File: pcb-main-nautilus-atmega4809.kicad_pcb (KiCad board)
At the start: 4 copper layers, 68.6 x 53.3 mm, 110 parts, among them J1 694106301002, J2 105017-0001, J3 FTSH-105-01-L-DV-007-K, J4 75844-101-06LF, J5 66951-006LF, J6 66951-010LF, J7 66951-008LF, J8 66951-008LF, Q1 BSS138PW, Q2 BSS138PW, Q3 BSS138PW, SW1 PTS645SH43SMTR92 LFS, U1 NCP1117-5.0_TO252, U2 AP2112K-3.3, U3 ATSAMD11D14A-SS, U4 ATmega4809-A

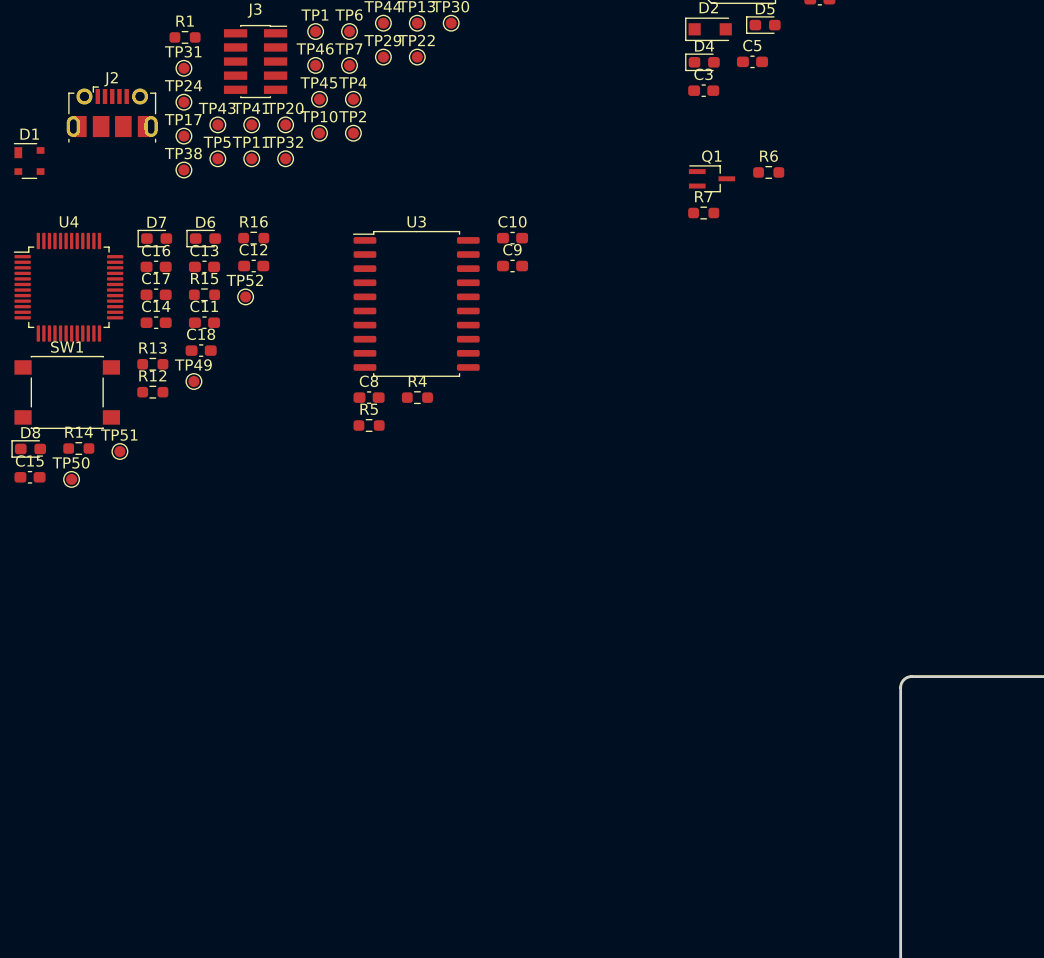
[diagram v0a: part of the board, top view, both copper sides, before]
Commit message: Place USB connector
Supports #4.
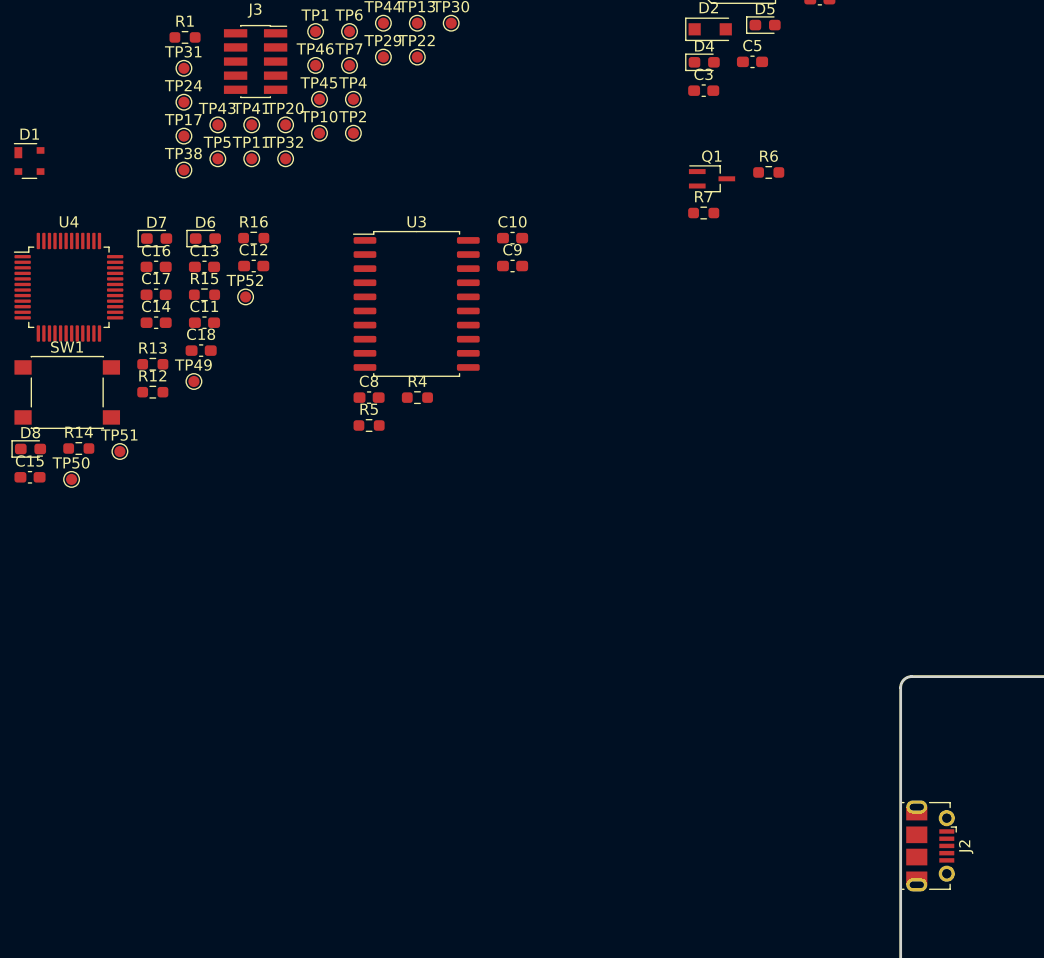
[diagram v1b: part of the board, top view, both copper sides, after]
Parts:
- moved J2 98.9 mm to (102.7, 111.9), turned to -90 degrees
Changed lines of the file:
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@@
     )
   )
-  (footprint "Connector_USB:USB_Micro-B_Molex-105017-0001" (layer "F.Cu")
-    (at 29.06 45.93)
+  (footprint "Connector_USB:USB_Micro-B_Molex-105017-0001" locked (layer "F.Cu")
+    (at 102.689204 111.9 -90)
     (descr "http://www.molex.com/pdm_docs/sd/1050170001_sd.pdf")
     (tags "Micro-USB SMD Typ-B")
@@
     (property "Sheetname" "")
     (attr smd)
-    (fp_text reference "J2" (at 0 -3.1125) (layer "F.SilkS")
+    (fp_text reference "J2" (at 0 -3.1125 90) (layer "F.SilkS")
       (effects (font (size 1 1) (thickness 0.15)))
     )
-    (fp_text value "105017-0001" (at 0.3 4.3375) (layer "F.Fab")
+    (fp_text value "105017-0001" (at 0.3 4.3375 90) (layer "F.Fab")
       (effects (font (size 1 1) (thickness 0.15)))
     )
-    (fp_text user "PCB Edge" (at 0 2.6875) (layer "Dwgs.User")
+    (fp_text user "PCB Edge" (at 0 2.6875 90) (layer "Dwgs.User")
       (effects (font (size 0.5 0.5) (thickness 0.08)))
     )
-    (fp_text user "${REFERENCE}" (at 0 0.8875) (layer "F.Fab")
+    (fp_text user "${REFERENCE}" (at 0 0.8875 90) (layer "F.Fab")
       (effects (font (size 1 1) (thickness 0.15)))
     )
@@
     (fp_line (start -1.1 -2.1225) (end -1.1 -1.9125) (layer "F.Fab") (width 0.1))
     (fp_line (start -3.75 -1.6125) (end 3.75 -1.6125) (layer "F.Fab") (width 0.1))
-    (pad "1" smd rect (at -1.3 -1.4625) (size 0.4 1.35) (layers "F.Cu" "F.Paste" "F.Mask")
+    (pad "1" smd rect locked (at -1.3 -1.4625 270) (size 0.4 1.35) (layers "F.Cu" "F.Paste" "F.Mask")
       (net 11 "/POWER/USB_VBUS") (pinfunction "VBUS") (pintype "power_out"))
-    (pad "2" smd rect (at -0.65 -1.4625) (size 0.4 1.35) (layers "F.Cu" "F.Paste" "F.Mask")
+    (pad "2" smd rect locked (at -0.65 -1.4625 270) (size 0.4 1.35) (layers "F.Cu" "F.Paste" "F.Mask")
       (net 9 "/UPDI PROGRAMMER AND USB-SERIAL BRIDGE/USB_D-") (pinfunction "D-") (pintype "bidirectional"))
-    (pad "3" smd rect (at 0 -1.4625) (size 0.4 1.35) (layers "F.Cu" "F.Paste" "F.Mask")
+    (pad "3" smd rect locked (at 0 -1.4625 270) (size 0.4 1.35) (layers "F.Cu" "F.Paste" "F.Mask")
       (net 10 "/UPDI PROGRAMMER AND USB-SERIAL BRIDGE/USB_D+") (pinfunction "D+") (pintype "bidirectional"))
-    (pad "4" smd rect (at 0.65 -1.4625) (size 0.4 1.35) (layers "F.Cu" "F.Paste" "F.Mask")
+    (pad "4" smd rect locked (at 0.65 -1.4625 270) (size 0.4 1.35) (layers "F.Cu" "F.Paste" "F.Mask")
       (net 19 "unconnected-(J2-Pad4)") (pinfunction "ID") (pintype "passive+no_connect"))
-    (pad "5" smd rect (at 1.3 -1.4625) (size 0.4 1.35) (layers "F.Cu" "F.Paste" "F.Mask")
+    (pad "5" smd rect locked (at 1.3 -1.4625 270) (size 0.4 1.35) (layers "F.Cu" "F.Paste" "F.Mask")
       (net 2 "/GND") (pinfunction "GND") (pintype "power_out"))
-    (pad "6" smd rect (at -1 1.2375) (size 1.5 1.9) (layers "F.Cu" "F.Paste" "F.Mask")
+    (pad "6" smd rect locked (at -1 1.2375 270) (size 1.5 1.9) (layers "F.Cu" "F.Paste" "F.Mask")
       (net 1 "Net-(C1-Pad1)") (pinfunction "Shield") (pintype "passive"))
-    (pad "6" smd rect (at 2.9 1.2375) (size 1.2 1.9) (layers "F.Cu" "F.Mask")
+    (pad "6" smd rect locked (at 2.9 1.2375 270) (size 1.2 1.9) (layers "F.Cu" "F.Mask")
       (net 1 "Net-(C1-Pad1)") (pinfunction "Shield") (pintype "passive"))
-    (pad "6" thru_hole oval (at 3.5 1.2375) (size 1.2 1.9) (drill oval 0.6 1.3) (layers *.Cu *.Mask)
+    (pad "6" thru_hole oval locked (at 3.5 1.2375 270) (size 1.2 1.9) (drill oval 0.6 1.3) (layers *.Cu *.Mask)
       (net 1 "Net-(C1-Pad1)") (pinfunction "Shield") (pintype "passive"))
-    (pad "6" smd rect (at 1 1.2375) (size 1.5 1.9) (layers "F.Cu" "F.Paste" "F.Mask")
+    (pad "6" smd rect locked (at 1 1.2375 270) (size 1.5 1.9) (layers "F.Cu" "F.Paste" "F.Mask")
       (net 1 "Net-(C1-Pad1)") (pinfunction "Shield") (pintype "passive"))
-    (pad "6" thru_hole circle (at 2.5 -1.4625) (size 1.45 1.45) (drill 0.85) (layers *.Cu *.Mask)
+    (pad "6" thru_hole circle locked (at 2.5 -1.4625 270) (size 1.45 1.45) (drill 0.85) (layers *.Cu *.Mask)
       (net 1 "Net-(C1-Pad1)") (pinfunction "Shield") (pintype "passive"))
-    (pad "6" thru_hole circle (at -2.5 -1.4625) (size 1.45 1.45) (drill 0.85) (layers *.Cu *.Mask)
+    (pad "6" thru_hole circle locked (at -2.5 -1.4625 270) (size 1.45 1.45) (drill 0.85) (layers *.Cu *.Mask)
       (net 1 "Net-(C1-Pad1)") (pinfunction "Shield") (pintype "passive"))
-    (pad "6" thru_hole oval (at -3.5 1.2375 180) (size 1.2 1.9) (drill oval 0.6 1.3) (layers *.Cu *.Mask)
+    (pad "6" thru_hole oval locked (at -3.5 1.2375 90) (size 1.2 1.9) (drill oval 0.6 1.3) (layers *.Cu *.Mask)
       (net 1 "Net-(C1-Pad1)") (pinfunction "Shield") (pintype "passive"))
-    (pad "6" smd rect (at -2.9 1.2375) (size 1.2 1.9) (layers "F.Cu" "F.Mask")
+    (pad "6" smd rect locked (at -2.9 1.2375 270) (size 1.2 1.9) (layers "F.Cu" "F.Mask")
       (net 1 "Net-(C1-Pad1)") (pinfunction "Shield") (pintype "passive"))
     (model "${KICAD6_3DMODEL_DIR}/Connector_USB.3dshapes/USB_Micro-B_Molex-105017-0001.wrl"

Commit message: Group components
Supports #4.
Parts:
- moved D8 239.4 mm to (260.4, 95.2)
- moved TP52 224.0 mm to (260.4, 108.0)
- moved R16 223.0 mm to (260.4, 101.6)
- moved TP51 220.2 mm to (247.7, 108.0)
- moved D7 218.8 mm to (248.5, 95.2)
- moved TP24 215.1 mm to (228.6, 139.7)
- moved R15 213.9 mm to (247.7, 101.6)
- moved TP50 211.6 mm to (234.9, 108.0)
- moved R14 211.4 mm to (235.9, 101.6)
- moved TP21 203.2 mm to (196.8, 171.4)
- moved D6 202.0 mm to (235.8, 95.2)
- moved TP23 199.7 mm to (228.6, 133.3)
- moved TP20 192.6 mm to (196.8, 165.1)
- moved SW1 192.4 mm to (215.9, 95.2)
- moved R13 188.8 mm to (215.9, 114.3)
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
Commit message: Add missing test points
Supports #4.
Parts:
- added TP49: TestPoint, TestPoint:TestPoint_Pad_D1.0mm, F.Cu at (171.4, 76.2)
- added TP50: TestPoint, TestPoint:TestPoint_Pad_D1.0mm, F.Cu at (171.4, 82.5)
- added TP51: TestPoint, TestPoint:TestPoint_Pad_D1.0mm, F.Cu at (171.4, 88.9)
- renumbered TP49 to TP52, TP50 to TP53, TP51 to TP54, TP52 to TP55
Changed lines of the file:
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@@
     (property "Sheetname" "MCU")
     (attr exclude_from_pos_files)
-    (fp_text reference "TP52" (at 0 -1.448) (layer "F.SilkS")
+    (fp_text reference "TP55" (at 0 -1.448) (layer "F.SilkS")
       (effects (font (size 1 1) (thickness 0.15)))
     )
@@
     (pad "1" smd circle (at 0 0) (size 1 1) (layers "F.Cu" "F.Mask")
       (net 41 "/MCU/D7") (pinfunction "1") (pintype "passive"))
+  )
+  (footprint "TestPoint:TestPoint_Pad_D1.0mm" (layer "F.Cu")
+    (at 171.45 82.55)
+    (descr "SMD pad as test Point, diameter 1.0mm")
+    (tags "test point SMD pad")
+    (property "Sheetfile" "pcb-main-nautilus-atmega4809-sheet-updi_programmer_and_usb_serial_bridge.kicad_sch")
+    (property "Sheetname" "UPDI PROGRAMMER AND USB-SERIAL BRIDGE")
+    (attr exclude_from_pos_files)
+    (fp_text reference "TP50" (at 0 -1.448) (layer "F.SilkS")
+      (effects (font (size 1 1) (thickness 0.15)))
+    )
+    (fp_text value "TestPoint" (at 0 1.55) (layer "F.Fab")
+      (effects (font (size 1 1) (thickness 0.15)))
+    )
+    (fp_text user "${REFERENCE}" (at 0 -1.45) (layer "F.Fab")
+      (effects (font (size 1 1) (thickness 0.15)))
+    )
+    (fp_circle (center 0 0) (end 0 0.7) (layer "F.SilkS") (width 0.12) (fill none))
+    (fp_circle (center 0 0) (end 1 0) (layer "F.CrtYd") (width 0.05) (fill none))
+    (pad "1" smd circle (at 0 0) (size 1 1) (layers "F.Cu" "F.Mask")
+      (net 51 "/UPDI PROGRAMMER AND USB-SERIAL BRIDGE/BI-DIRECTIONAL LEVEL SHIFTER: TX/SIGNAL_3.3V") (pinfunction "1") (pintype "passive"))
   )
   (footprint "Package_TO_SOT_SMD:SOT-23-5" (layer "F.Cu")
@@
     (property "Sheetname" "MCU")
     (attr exclude_from_pos_files)
-    (fp_text reference "TP51" (at 0 -1.448) (layer "F.SilkS")
+    (fp_text reference "TP54" (at 0 -1.448) (layer "F.SilkS")
       (effects (font (size 1 1) (thickness 0.15)))
     )
@@
   )
   (footprint "TestPoint:TestPoint_Pad_D1.0mm" (layer "F.Cu")
+    (at 171.45 88.9)
+    (descr "SMD pad as test Point, diameter 1.0mm")
+    (tags "test point SMD pad")
+    (property "Sheetfile" "pcb-main-nautilus-atmega4809-sheet-updi_programmer_and_usb_serial_bridge.kicad_sch")
+    (property "Sheetname" "UPDI PROGRAMMER AND USB-SERIAL BRIDGE")
+    (attr exclude_from_pos_files)
+    (fp_text reference "TP51" (at 0 -1.448) (layer "F.SilkS")
+      (effects (font (size 1 1) (thickness 0.15)))
+    )
+    (fp_text value "TestPoint" (at 0 1.55) (layer "F.Fab")
+      (effects (font (size 1 1) (thickness 0.15)))
+    )
+    (fp_text user "${REFERENCE}" (at 0 -1.45) (layer "F.Fab")
+      (effects (font (size 1 1) (thickness 0.15)))
+    )
+    (fp_circle (center 0 0) (end 0 0.7) (layer "F.SilkS") (width 0.12) (fill none))
+    (fp_circle (center 0 0) (end 1 0) (layer "F.CrtYd") (width 0.05) (fill none))
+    (pad "1" smd circle (at 0 0) (size 1 1) (layers "F.Cu" "F.Mask")
+      (net 50 "/UPDI PROGRAMMER AND USB-SERIAL BRIDGE/BI-DIRECTIONAL LEVEL SHIFTER: UPDI/SIGNAL_3.3V") (pinfunction "1") (pintype "passive"))
+  )
+  (footprint "TestPoint:TestPoint_Pad_D1.0mm" (layer "F.Cu")
     (at 19.05 82.55)
     (descr "SMD pad as test Point, diameter 1.0mm")
@@
   )
   (footprint "TestPoint:TestPoint_Pad_D1.0mm" (layer "F.Cu")
+    (at 171.45 76.2)
+    (descr "SMD pad as test Point, diameter 1.0mm")
+    (tags "test point SMD pad")
+    (property "Sheetfile" "pcb-main-nautilus-atmega4809-sheet-updi_programmer_and_usb_serial_bridge.kicad_sch")
+    (property "Sheetname" "UPDI PROGRAMMER AND USB-SERIAL BRIDGE")
+    (attr exclude_from_pos_files)
+    (fp_text reference "TP49" (at 0 -1.448) (layer "F.SilkS")
+      (effects (font (size 1 1) (thickness 0.15)))
+    )
+    (fp_text value "TestPoint" (at 0 1.55) (layer "F.Fab")
+      (effects (font (size 1 1) (thickness 0.15)))
+    )
+    (fp_text user "${REFERENCE}" (at 0 -1.45) (layer "F.Fab")
+      (effects (font (size 1 1) (thickness 0.15)))
+    )
+    (fp_circle (center 0 0) (end 0 0.7) (layer "F.SilkS") (width 0.12) (fill none))
+    (fp_circle (center 0 0) (end 1 0) (layer "F.CrtYd") (width 0.05) (fill none))
+    (pad "1" smd circle (at 0 0) (size 1 1) (layers "F.Cu" "F.Mask")
+      (net 53 "/UPDI PROGRAMMER AND USB-SERIAL BRIDGE/BI-DIRECTIONAL LEVEL SHIFTER: RX/SIGNAL_3.3V") (pinfunction "1") (pintype "passive"))
+  )
+  (footprint "TestPoint:TestPoint_Pad_D1.0mm" (layer "F.Cu")
     (at 158.75 63.5)
     (descr "SMD pad as test Point, diameter 1.0mm")
@@
     (property "Sheetname" "MCU")
     (attr exclude_from_pos_files)
-    (fp_text reference "TP49" (at 0 -1.448) (layer "F.SilkS")
+    (fp_text reference "TP52" (at 0 -1.448) (layer "F.SilkS")
       (effects (font (size 1 1) (thickness 0.15)))
     )
@@
     (property "Sheetname" "MCU")
     (attr exclude_from_pos_files)
-    (fp_text reference "TP50" (at 0 -1.448) (layer "F.SilkS")
-      (effects (font (size 1 1) (thickness 0.15)))
-    )
+    (fp_text reference "TP53" (at 0 -1.448) (layer "F.SilkS")
+      (effects (font (size 1 1) (thickness 0.15)))
+    )

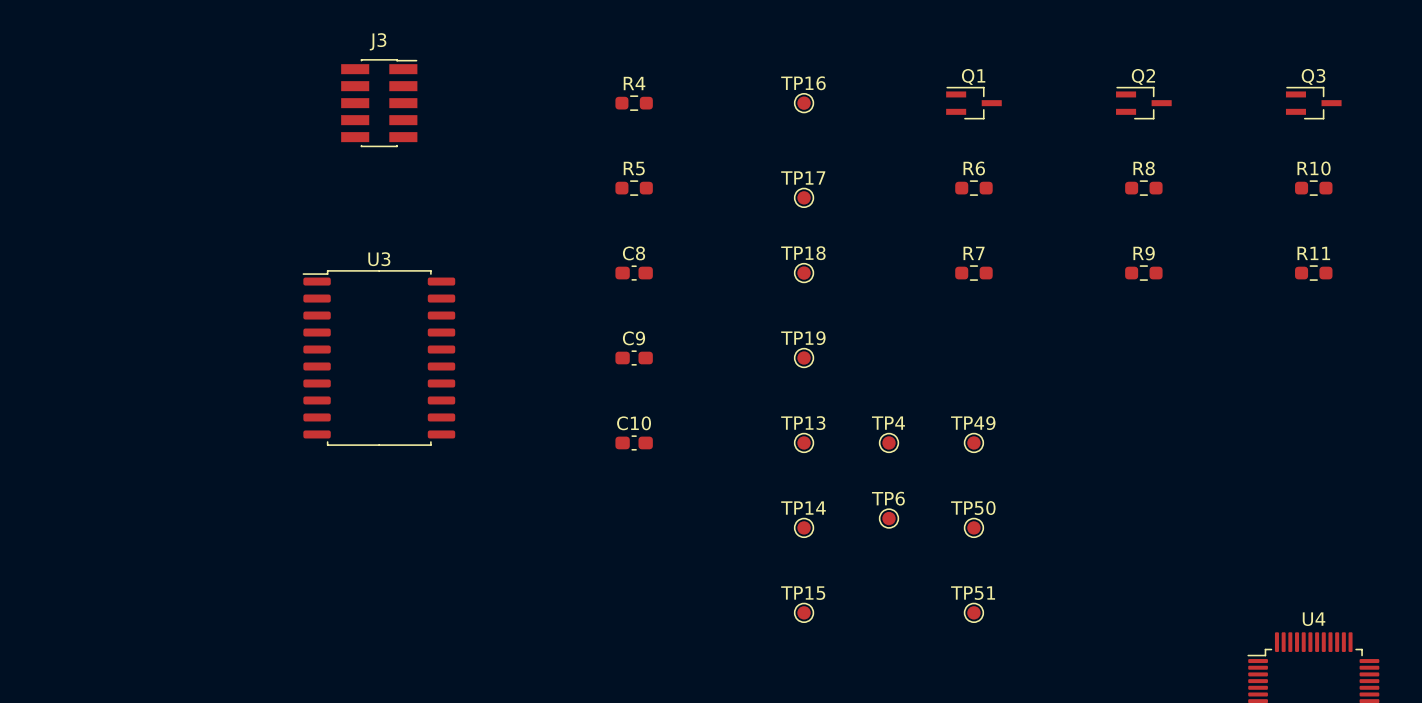
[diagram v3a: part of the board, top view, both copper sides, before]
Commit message: Arrange USB programmer and USB-serial bridge components
Supports #4.
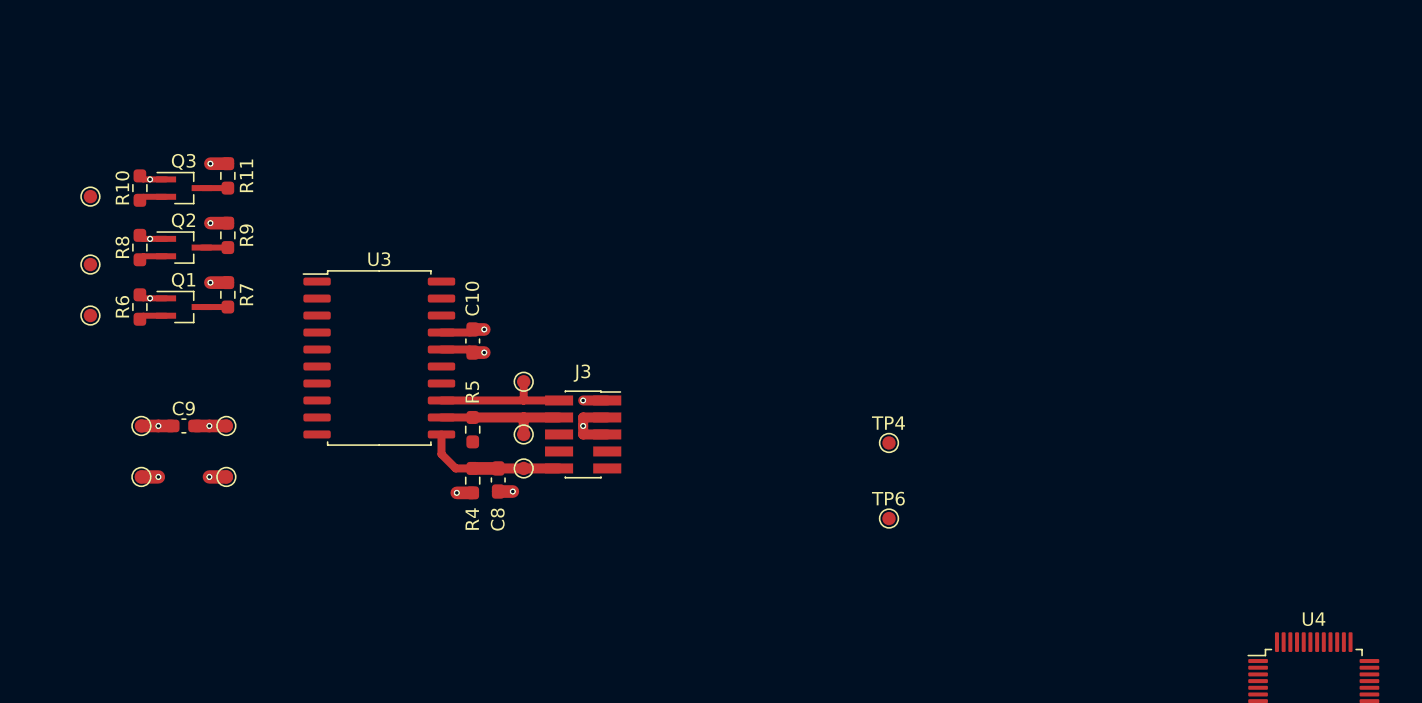
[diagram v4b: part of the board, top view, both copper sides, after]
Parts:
- moved R10 87.7 mm to (109.1, 57.1), turned to -90 degrees
- moved Q3 84.7 mm to (112.4, 57.1)
- moved R11 81.5 mm to (115.7, 56.2), turned to -90 degrees
- moved R8 75.2 mm to (109.1, 61.6), turned to -90 degrees
- moved Q2 72.6 mm to (112.4, 61.6)
- moved TP51 69.7 mm to (105.4, 66.7)
- moved TP50 68.9 mm to (105.4, 62.9)
- moved TP49 68.6 mm to (105.4, 57.8)
- moved R9 68.5 mm to (115.7, 60.7), turned to -90 degrees
- moved R6 63.0 mm to (109.1, 66.0), turned to -90 degrees
- moved Q1 61.0 mm to (112.4, 66.0)
- moved TP16 56.9 mm to (109.2, 78.7)
- moved R7 55.8 mm to (115.7, 65.1), turned to -90 degrees
- moved TP19 49.8 mm to (109.2, 74.9), turned to -90 degrees
- moved TP17 48.0 mm to (115.6, 78.7)
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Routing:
- net /3.3V: track 0.00 -> 14.8 mm, vias 0 -> 7
- net /GND: track 0.00 -> 12.8 mm, vias 0 -> 5
- net /UPDI PROGRAMMER AND USB-SERIAL BRIDGE/~{RESET}: track 0.00 -> 10.7 mm
- net /UPDI PROGRAMMER AND USB-SERIAL BRIDGE/SWD_SWDIO: track 0.00 -> 10.2 mm
- net /UPDI PROGRAMMER AND USB-SERIAL BRIDGE/SWD_SWCLK: track 0.00 -> 10.1 mm
- net /5V: track 0.00 -> 5.18 mm, vias 0 -> 4
- net /UPDI PROGRAMMER AND USB-SERIAL BRIDGE/BI-DIRECTIONAL LEVEL SHIFTER: UPDI/SIGNAL_3.3V: track 0.00 -> 2.07 mm
- net /UPDI PROGRAMMER AND USB-SERIAL BRIDGE/BI-DIRECTIONAL LEVEL SHIFTER: TX/SIGNAL_3.3V: track 0.00 -> 2.07 mm
- net /UPDI PROGRAMMER AND USB-SERIAL BRIDGE/BI-DIRECTIONAL LEVEL SHIFTER: RX/SIGNAL_3.3V: track 0.00 -> 2.07 mm
- net /MCU/UPDI: track 0.00 -> 1.96 mm
- net /MCU/TX: track 0.00 -> 1.96 mm
- net /MCU/RX: track 0.00 -> 1.96 mm
